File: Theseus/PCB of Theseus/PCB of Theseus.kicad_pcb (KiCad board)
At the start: 2 copper layers, 135 x 80 mm, 127 parts, among them J1 TB001-500-04BE, J11 TB002-500-02BE, J12 TB002-500-02BE, J2 TB001-500-04BE, J3 TB002-500-02BE, J4 TB003-500-P06BE, J5 CN4 STDC14 (Programmer), J6 Micro SD Holder 0472192001, J7 TB002-500-02BE, J8 TB003-500-P06BE, Q1 DMG1012UW-7, Q2 DMG1012UW-7, U1 TPS565201DDC, U11 INA326, U12 INA326, U13 MAX6675, U2 MCP2562, U3 INA326, U4 INA326, U5 MX25L25645G, U6 STM32H750VBTx, Y1 ASE-4.000MHz-L-C-T

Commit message: Flight design, first pass
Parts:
- removed C20, C21: 0.5n, Capacitor_SMD:C_0805_2012Metric_Pad1.18x1.45mm_HandSolder
- removed C23, C28, C29, C34: 0.47u, Capacitor_SMD:C_0805_2012Metric_Pad1.18x1.45mm_HandSolder
- removed C27, C33: 0.047u, Capacitor_SMD:C_0805_2012Metric_Pad1.18x1.45mm_HandSolder
- removed C30, C31: 2n, Capacitor_SMD:C_0805_2012Metric_Pad1.18x1.45mm_HandSolder
- removed C36, C37, C38, C39: 0.1u, Capacitor_SMD:C_0805_2012Metric_Pad1.18x1.45mm_HandSolder
- removed J11, J12: TB002-500-02BE, TerminalBlock_CUI:TerminalBlock_CUI_TB007-508-02_1x02_P5.08mm_Horizontal
- removed J8: TB003-500-P06BE, TerminalBlock_CUI:TerminalBlock_CUI_TB007-508-06_1x06_P5.08mm_Horizontal
- removed R18, R19: 32.4k ±0.1%, Resistor_SMD:R_0805_2012Metric_Pad1.20x1.40mm_HandSolder
- removed R20: 100R ±0.1%, Resistor_SMD:R_0805_2012Metric_Pad1.20x1.40mm_HandSolder
- removed R21, R38: 8.06k, Resistor_SMD:R_0805_2012Metric_Pad1.20x1.40mm_HandSolder
- removed R22, R23: 200k, Resistor_SMD:R_0805_2012Metric_Pad1.20x1.40mm_HandSolder
- removed R24, R25, R30: 1M ±0.1%, Resistor_SMD:R_0805_2012Metric_Pad1.20x1.40mm_HandSolder
- removed R26, R31, R32, R37: 806R, Resistor_SMD:R_0805_2012Metric_Pad1.20x1.40mm_HandSolder
- removed R29: 10M ±1%, Resistor_SMD:R_0805_2012Metric_Pad1.20x1.40mm_HandSolder
- removed R33, R35: 20k, Resistor_SMD:R_0805_2012Metric_Pad1.20x1.40mm_HandSolder
- removed R34, R36: 80.6k, Resistor_SMD:R_0805_2012Metric_Pad1.20x1.40mm_HandSolder
- removed TH1: PTS060301B100RP100, Resistor_SMD:R_0603_1608Metric_Pad0.98x0.95mm_HandSolder
- removed TP2: TC2+, TestPoint:TestPoint_Pad_D2.0mm
- removed TP3: TC2-, TestPoint:TestPoint_Pad_D2.0mm
- removed TP6: TC3+, TestPoint:TestPoint_Pad_D2.0mm
- removed TP7: TC3-, TestPoint:TestPoint_Pad_D2.0mm
- removed TP8: RTD1, TestPoint:TestPoint_Pad_D2.0mm
- removed TP9: RTD2, TestPoint:TestPoint_Pad_D2.0mm
- removed U11, U12, U3, U4: INA326, Package_SO:MSOP-8_3x3mm_P0.65mm
- C1, C2, C22, C25, C3, C32, C6, C7, C8, D1, D5, L1, Q1, Q2, R1, R11, R12, R2, R27, R28, R3, R46, R47, R5, R6, U1, U2: moved to B.Cu
- C26: moved to F.Cu
- J1, J2: value TB001-500-04BE -> Conn_01x06_Socket; footprint TerminalBlock_CUI:TerminalBlock_CUI_TB007-508-04_1x04_P5.08mm_Horizontal -> canhw_footprints:connector_Harwin_G125–MG10605M4P
- J3: value TB002-500-02BE -> G125-MH104M4-04AD000P; footprint TerminalBlock_CUI:TerminalBlock_CUI_TB007-508-02_1x02_P5.08mm_Horizontal -> canhw_footprints:connector_Harwin_G125-MH104M4-04AD000P
- J4: value TB003-500-P06BE -> Conn_01x06_Socket; footprint TerminalBlock_CUI:TerminalBlock_CUI_TB007-508-06_1x06_P5.08mm_Horizontal -> canhw_footprints:connector_Harwin_G125–MG10605M4P
- R13, R14, R15, R16, R17: value 50k -> 51k
- moved H6 101.0 mm to (184.3, 49.8)
- moved J7 86.1 mm to (182.0, 64.0), turned to 90 degrees
- moved TP10 85.8 mm to (175.8, 74.5), turned to 0 degrees
- moved H8 85.2 mm to (123.2, 89.1)
- moved TP1 84.6 mm to (175.6, 69.8), turned to 0 degrees
- moved L1 84.5 mm to (169.9, 82.7), turned to 180 degrees
- moved R11 79.5 mm to (169.9, 78.8), turned to 0 degrees
- moved C3 76.9 mm to (170.0, 75.5), turned to 0 degrees
- moved D5 75.7 mm to (141.3, 90.8)
- moved G*** 75.1 mm to (182.4, 72.8), turned to 90 degrees
- moved J1 71.5 mm to (138.2, 87.3)
- moved R12 71.4 mm to (170.9, 67.1), turned to 0 degrees
- moved D1 71.2 mm to (136.1, 90.8)
- moved U1 71.1 mm to (169.9, 71.1), turned to 0 degrees
- moved C24 70.8 mm to (166.6, 50.1)
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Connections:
- J2 pad 1: +5V -> +3.3V
- J2 pad 2: GND -> /MCU/HALL_1
- J2 pad 3: /CANH -> GND
- J2 pad 4: /CANL -> +3.3V
- J3 pad 1: Net-(J3-Pin_1) -> /CANH
- J3 pad 2: Net-(J3-Pin_2) -> /CANL
- TP4 pad 1: Net-(J12-Pin_2) -> /Valves and Sensors/TC1+
- TP5 pad 1: Net-(J12-Pin_1) -> /Valves and Sensors/TC1-
- U13 pad 2: Net-(J12-Pin_2) -> /Valves and Sensors/TC1+
- U13 pad 3: Net-(J12-Pin_1) -> /Valves and Sensors/TC1-
- U6 pad 1: /MCU/TC2+ -> unconnected-(U6-PE2-Pad1)
- U6 pad 2: /MCU/TC2- -> unconnected-(U6-PE3-Pad2)
- U6 pad 3: /MCU/TC3 -> unconnected-(U6-PE4-Pad3)
- U6 pad 35: /MCU/PT_2 -> /MCU/PT_1
- U6 pad 36: /MCU/PT_1 -> /MCU/PT_2
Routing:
- net +BATT: track 180.9 -> 76.7 mm, vias 0 -> 2
- net /MCU/VALVE_2: track 61.2 -> 5.38 mm, vias 0 -> 1
- net /MCU/TC3: track 43.4 -> 0.00 mm
- net /MCU/VALVE_1: track 43.7 -> 5.40 mm, vias 0 -> 1
- net /Valves and Sensors/TC1+: track 0.00 -> 31.3 mm
- net Net-(C21-Pad2): track 25.1 -> 0.00 mm
- net /MCU/TCK: track 13.4 -> 37.4 mm
- net +3.3V: track 152.3 -> 128.5 mm, vias 29 -> 14
- net /MCU/TC2+: track 23.0 -> 0.00 mm
- net /MCU/V_BATT: track 60.7 -> 37.8 mm, vias 0 -> 1
- net /CAN_Rx: track 27.1 -> 4.45 mm, vias 0 -> 1
- net GND: track 128.5 -> 148.5 mm, vias 11 -> 19
- net /CAN_Tx: track 22.6 -> 3.60 mm, vias 0 -> 1
- net /MCU/OSC_IN: track 22.7 -> 4.25 mm
- net /Valves and Sensors/TC1-: track 0.00 -> 18.2 mm
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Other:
- board size 135 x 80 mm -> 72.5 x 50 mm
- board text added: "PCB OF THESEUS FLIGHT EDITION REV 3"
- board text removed: "+3.3V"
- board text removed: "3.3V"
- board text removed: "5V"
- board text removed: "BATT+"
- board text removed: "CANH"
- board text removed: "CANL"
- board text removed: "CLK"
- board text removed: "DI"
- board text removed: "DO"
- board text removed: "GND"
- board text removed: "HALL"
- board text removed: "HALL 1"
- board text removed: "HALL 2"
- board text removed: "IF YOU'RE READING THIS THE PCB IS UPSIDE-DOWN (OR YOU'RE IN THE SHADOW REALM)"
- board text removed: "PCB OF THESEUS DEV EDITION, REV 2"
- board text removed: "PT1+"
- board text removed: "PT1-"
- board text removed: "PT2+"
- board text removed: "PT2-"
- board text removed: "PT3+"
- board text removed: "PT3-"
- board text removed: "RST"
- board text removed: "RTD+"
- board text removed: "RTD-"
- board text removed: "TC1+"
- board text removed: "TC1-"
- board text removed: "TC2+"
- board text removed: "TC2-"
- board text removed: "TC3+"
- board text removed: "TC3-"
- board text removed: "TMS"
- board text removed: "V1+"
- board text removed: "V1-"
- board text removed: "V2+"
- board text removed: "V2-"
- board text removed: "VCP_RX"
- board text removed: "VCP_TX"

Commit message: Flight design v1
First pass at flight design
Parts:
- removed the G*** at (182.4, 72.8)
- removed the G*** at (152.1, 50.5)
- removed J4: Conn_01x06_Socket, canhw_footprints:connector_Harwin_G125–MG10605M4P
- added G***: LOGO, Team_Logo:Logo_SilkScreen_5mm, F.Cu at (152.9, 111.5)
- added J8: Conn_01x12_Socket, canhw_footprints:connector_Harwin_G125-MV11205M1P, F.Cu at (139.5, 117.5)
- added R10: 82K, Resistor_SMD:R_0603_1608Metric_Pad0.98x0.95mm_HandSolder, F.Cu at (145.1, 112.8)
- added R18: 130K, Resistor_SMD:R_0603_1608Metric_Pad0.98x0.95mm_HandSolder, B.Cu at (146.7, 112.8)
- added R19: 82K, Resistor_SMD:R_0603_1608Metric_Pad0.98x0.95mm_HandSolder, F.Cu at (142.3, 112.4)
- added R20: 130K, Resistor_SMD:R_0603_1608Metric_Pad0.98x0.95mm_HandSolder, B.Cu at (144.2, 112.9)
- added R8: 82K, Resistor_SMD:R_0603_1608Metric_Pad0.98x0.95mm_HandSolder, F.Cu at (147.2, 112.9)
- added R9: 130K, Resistor_SMD:R_0603_1608Metric_Pad0.98x0.95mm_HandSolder, B.Cu at (149.4, 112.9)
- C1, C11, C12, C16, C18, C19, C2, C24, C25, C3, C32, C35, C4, C5, C6: footprint Capacitor_SMD:C_0805_2012Metric_Pad1.18x1.45mm_HandSolder -> Capacitor_SMD:C_0603_1608Metric_Pad1.08x0.95mm_HandSolder
- C10, C13, C14, C15, C17, C26, C40, C9: footprint Capacitor_SMD:C_0805_2012Metric_Pad1.18x1.45mm_HandSolder -> Capacitor_SMD:C_0603_1608Metric_Pad1.08x0.95mm_HandSolder; moved to B.Cu
- C22, C7, C8: footprint Capacitor_SMD:C_0805_2012Metric_Pad1.18x1.45mm_HandSolder -> Capacitor_SMD:C_0603_1608Metric_Pad1.08x0.95mm_HandSolder; moved to F.Cu
- D2, D6: footprint Diode_SMD:D_1206_3216Metric_Pad1.42x1.75mm_HandSolder -> Diode_SMD:D_0603_1608Metric_Pad1.05x0.95mm_HandSolder
- F1, FB1, U13, U5, Y1: moved to B.Cu
- J5: footprint Connector_PinHeader_1.27mm:PinHeader_2x07_P1.27mm_Vertical_SMD -> Connector_PinSocket_1.27mm:PinSocket_2x07_P1.27mm_Vertical_SMD
- J7: value TB002-500-02BE -> 4DB-P108-02; footprint TerminalBlock_CUI:TerminalBlock_CUI_TB007-508-02_1x02_P5.08mm_Horizontal -> canhw_footprints:4DB-P108-02
- Q1, Q2: moved to F.Cu
- R1, R11, R12, R13, R14, R15, R16, R17, R2, R3, R4, R7: footprint Resistor_SMD:R_0805_2012Metric_Pad1.20x1.40mm_HandSolder -> Resistor_SMD:R_0603_1608Metric_Pad0.98x0.95mm_HandSolder
- R27, R28, R5, R6: footprint Resistor_SMD:R_0805_2012Metric_Pad1.20x1.40mm_HandSolder -> Resistor_SMD:R_0603_1608Metric_Pad0.98x0.95mm_HandSolder; moved to F.Cu
- R44, R45: footprint Resistor_SMD:R_0805_2012Metric_Pad1.20x1.40mm_HandSolder -> Resistor_SMD:R_0603_1608Metric_Pad0.98x0.95mm_HandSolder; moved to B.Cu
- R46: value 3M ±1% -> 300K; footprint Resistor_SMD:R_0805_2012Metric_Pad1.20x1.40mm_HandSolder -> Resistor_SMD:R_0603_1608Metric_Pad0.98x0.95mm_HandSolder
- R47: value 1M ±0.1% -> 100K; footprint Resistor_SMD:R_0805_2012Metric_Pad1.20x1.40mm_HandSolder -> Resistor_SMD:R_0603_1608Metric_Pad0.98x0.95mm_HandSolder
- moved H6 90.1 mm to (121.0, 114.0)
- moved H5 85.1 mm to (179.0, 114.0)
- moved C16 68.2 mm to (161.6, 118.0), turned to 0 degrees
- moved C24 65.2 mm to (165.2, 115.3), turned to 0 degrees
- moved C4 63.8 mm to (165.2, 118.0), turned to 0 degrees
- moved C17 61.8 mm to (130.6, 105.1), turned to 0 degrees
- moved C5 61.0 mm to (161.6, 115.3), turned to 180 degrees
- moved C11 60.2 mm to (137.6, 110.5), turned to 0 degrees
- moved C35 58.1 mm to (124.7, 92.4)
- moved C12 57.9 mm to (151.1, 107.2), turned to 0 degrees
- moved R46 57.3 mm to (152.4, 117.0), turned to 90 degrees
- moved C26 57.3 mm to (162.1, 106.8), turned to 180 degrees
- moved R47 56.3 mm to (152.4, 112.6), turned to 90 degrees
- moved C40 53.4 mm to (141.5, 99.1), turned to 0 degrees
- moved TP1 48.1 mm to (168.6, 117.4)
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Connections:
- net /MCU/PT_3 renamed /Valves and Sensors/PT3_OUT
- R1 pad 1: /MCU/PT_1 -> /Valves and Sensors/PT1_OUT
- R2 pad 1: /MCU/PT_2 -> /Valves and Sensors/PT2_OUT
- U6 pad 35: /MCU/PT_1 -> /Valves and Sensors/PT2_OUT
- U6 pad 36: /MCU/PT_2 -> /Valves and Sensors/PT1_OUT
- U6 pad 40: unconnected-(U6-PE10-Pad40) -> /MCU/PT6
- U6 pad 41: unconnected-(U6-PE11-Pad41) -> /MCU/PT5
- U6 pad 42: unconnected-(U6-PE12-Pad42) -> /MCU/PT4
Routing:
- net GND: track 148.5 -> 34.1 mm, vias 19 -> 9
- net +BATT: track 76.7 -> 130.2 mm, vias 2 -> 0
- net /MCU/VCP_RX: track 5.05 -> 36.8 mm, vias 0 -> 2
- net +3.3V: track 128.5 -> 100.5 mm, vias 14 -> 24
- net /MCU/TCK: track 37.4 -> 12.3 mm, vias 2 -> 0
- net +5V: track 42.8 -> 17.7 mm
- net /CANL: track 26.6 -> 2.66 mm
- net /MCU/PT_1: track 23.9 -> 0.00 mm, vias 1 -> 0
- net /MCU/VCP_TX: track 7.69 -> 30.9 mm, vias 0 -> 2
- net /MCU/TMS: track 32.4 -> 9.97 mm, vias 0 -> 2
- net /CANH: track 25.1 -> 2.67 mm
- net /MCU/SD_CMD: track 22.4 -> 44.6 mm
- net /MCU/PT_2: track 21.8 -> 0.00 mm, vias 1 -> 0
- net /MCU/SD_D3: track 19.0 -> 40.2 mm
- net /MCU/V_BATT: track 37.8 -> 17.6 mm
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- added copper zone on In2.Cu, net +3.3V
- added copper zone on B.Cu, net GND
- added copper zone on In1.Cu, net GND
- removed copper zone on B.Cu, net +3.3V
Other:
- board size 72.5 x 50 mm -> 70 x 40 mm
- copper layers 2 -> 4
- board text added: "PCB OF THESEUS REV 3 MATTHEW GORDON"
- board text added: "TCK"
- board text added: "TDI"
- board text added: "TDO"
- board text added: "TMS"
- board text added: "TRST"
- board text added: "VALVE 1"
- board text added: "VALVE 2"
- board text added: "VCPRX"
- board text added: "VCPTX"
- board text removed: "MATTHEW GORDON"
- board text removed: "PCB OF THESEUS FLIGHT EDITION REV 3"

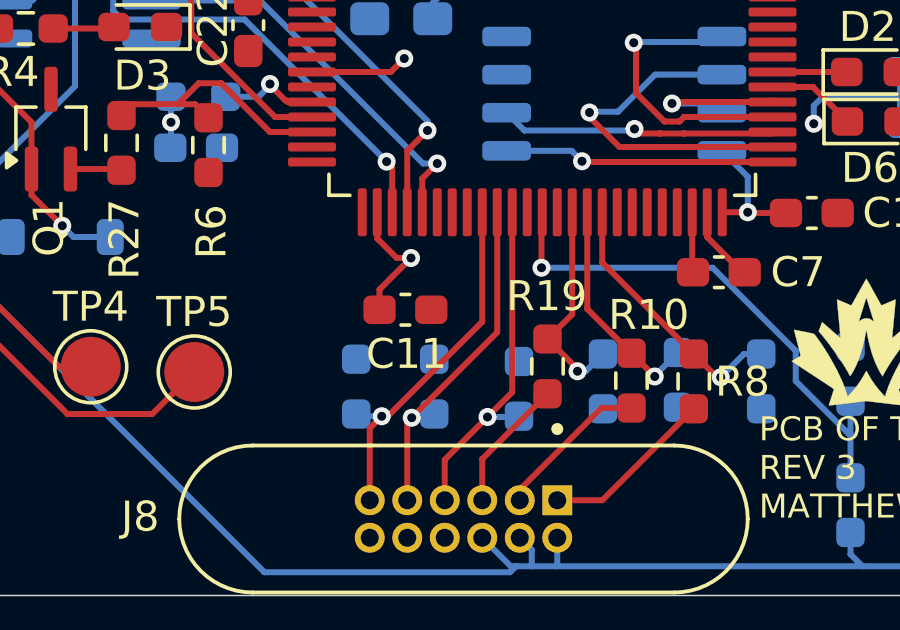
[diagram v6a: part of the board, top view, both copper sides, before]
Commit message: Fix PT3 ADC
Updated PT3 to use valid ADC pin
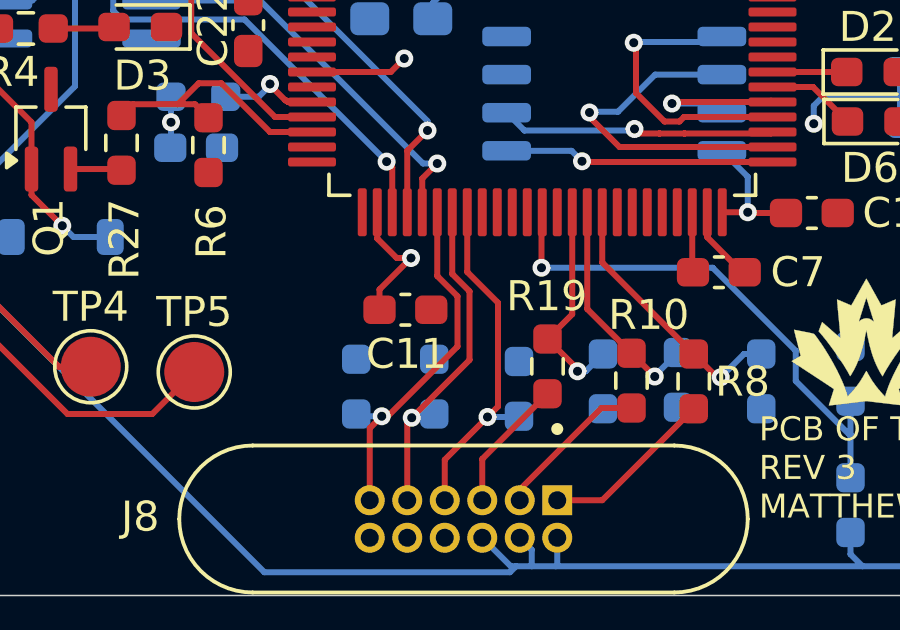
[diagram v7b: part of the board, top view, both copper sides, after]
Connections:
- U6 pad 31: unconnected-(U6-PA7-Pad31) -> /Valves and Sensors/PT3_OUT
- U6 pad 32: unconnected-(U6-PC4-Pad32) -> /Valves and Sensors/PT2_OUT
- U6 pad 33: unconnected-(U6-PC5-Pad33) -> /Valves and Sensors/PT1_OUT
- U6 pad 34: /Valves and Sensors/PT3_OUT -> unconnected-(U6-PB0-Pad34)
- U6 pad 35: /Valves and Sensors/PT2_OUT -> unconnected-(U6-PB1-Pad35)
- U6 pad 36: /Valves and Sensors/PT1_OUT -> unconnected-(U6-PB2-Pad36)
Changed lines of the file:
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@@
 	(net 42 "Net-(U1-VBST)")
 	(net 43 "unconnected-(U6-PC3_C-Pad18)")
-	(net 44 "unconnected-(U6-PC5-Pad33)")
+	(net 44 "unconnected-(U6-PB0-Pad34)")
 	(net 45 "unconnected-(U6-PB7-Pad93)")
 	(net 46 "unconnected-(U6-PC0-Pad15)")
-	(net 47 "unconnected-(U6-PC4-Pad32)")
+	(net 47 "unconnected-(U6-PB2-Pad36)")
 	(net 48 "unconnected-(U6-PE0-Pad97)")
 	(net 49 "unconnected-(U6-PA11-Pad70)")
@@
 	(net 90 "unconnected-(U6-PE7-Pad37)")
 	(net 91 "unconnected-(U6-PE4-Pad3)")
-	(net 92 "unconnected-(U6-PA7-Pad31)")
+	(net 92 "unconnected-(U6-PB1-Pad35)")
 	(net 93 "unconnected-(U6-PA2-Pad24)")
 	(net 94 "unconnected-(J3-NC-Pad4)")
@@
 			(layers "F.Cu" "F.Mask" "F.Paste")
 			(roundrect_rratio 0.25)
-			(net 92 "unconnected-(U6-PA7-Pad31)")
+			(net 114 "/Valves and Sensors/PT3_OUT")
 			(pinfunction "PA7")
-			(pintype "bidirectional+no_connect")
+			(pintype "bidirectional")
 		)
 		(pad "32" smd roundrect
@@
 			(layers "F.Cu" "F.Mask" "F.Paste")
 			(roundrect_rratio 0.25)
-			(net 47 "unconnected-(U6-PC4-Pad32)")
+			(net 113 "/Valves and Sensors/PT2_OUT")
 			(pinfunction "PC4")
-			(pintype "bidirectional+no_connect")
+			(pintype "bidirectional")
 		)
 		(pad "33" smd roundrect
@@
 			(layers "F.Cu" "F.Mask" "F.Paste")
 			(roundrect_rratio 0.25)
-			(net 44 "unconnected-(U6-PC5-Pad33)")
+			(net 112 "/Valves and Sensors/PT1_OUT")
 			(pinfunction "PC5")
-			(pintype "bidirectional+no_connect")
+			(pintype "bidirectional")
 		)
 		(pad "34" smd roundrect
@@
 			(layers "F.Cu" "F.Mask" "F.Paste")
 			(roundrect_rratio 0.25)
-			(net 114 "/Valves and Sensors/PT3_OUT")
+			(net 44 "unconnected-(U6-PB0-Pad34)")
 			(pinfunction "PB0")
-			(pintype "bidirectional")
+			(pintype "bidirectional+no_connect")
 		)
 		(pad "35" smd roundrect
@@
 			(layers "F.Cu" "F.Mask" "F.Paste")
 			(roundrect_rratio 0.25)
-			(net 113 "/Valves and Sensors/PT2_OUT")
+			(net 92 "unconnected-(U6-PB1-Pad35)")
 			(pinfunction "PB1")
-			(pintype "bidirectional")
+			(pintype "bidirectional+no_connect")
 		)
 		(pad "36" smd roundrect
@@
 			(layers "F.Cu" "F.Mask" "F.Paste")
 			(roundrect_rratio 0.25)
-			(net 112 "/Valves and Sensors/PT1_OUT")
+			(net 47 "unconnected-(U6-PB2-Pad36)")
 			(pinfunction "PB2")
-			(pintype "bidirectional")
+			(pintype "bidirectional+no_connect")
 		)
 		(pad "37" smd roundrect
@@
 	)
 	(segment
-		(start 141.15 113.225)
-		(end 141.15 107.225)
+		(start 140.325 114.05)
+		(end 138.9 115.475)
+		(width 0.2)
+		(layer "F.Cu")
+		(net 112)
+	)
+	(segment
+		(start 138.9 115.475)
+		(end 138.9 116.825)
 		(width 0.2)
 		(layer "F.Cu")
@@
 	(segment
 		(start 140.325 114.05)
-		(end 138.9 115.475)
+		(end 140.675 113.7)
 		(width 0.2)
 		(layer "F.Cu")
@@
 	)
 	(segment
-		(start 138.9 115.475)
-		(end 138.9 116.825)
+		(start 140.675 110.2408)
+		(end 140.675 113.7)
 		(width 0.2)
 		(layer "F.Cu")
@@
 	)
 	(segment
-		(start 140.325 114.05)
-		(end 141.15 113.225)
+		(start 139.65 107.225)
+		(end 139.65 109.2158)
+		(width 0.2)
+		(layer "F.Cu")
+		(net 112)
+	)
+	(segment
+		(start 139.65 109.2158)
+		(end 140.675 110.2408)
 		(width 0.2)
 		(layer "F.Cu")
@@
 	)
 	(segment
-		(start 140.65 111.225)
-		(end 140.65 107.225)
+		(start 139.15 107.225)
+		(end 139.15 109.2829)
+		(width 0.2)
+		(layer "F.Cu")
+		(net 113)
+	)
+	(segment
+		(start 139.726 109.8589)
+		(end 139.726 112.149)
 		(width 0.2)
 		(layer "F.Cu")
@@
 	(segment
 		(start 137.8 114.075)
-		(end 140.65 111.225)
+		(end 139.726 112.149)
 		(width 0.2)
 		(layer "F.Cu")
@@
 	)
 	(segment
+		(start 139.15 109.2829)
+		(end 139.726 109.8589)
+		(width 0.2)
+		(layer "F.Cu")
+		(net 113)
+	)
+	(segment
 		(start 137.8 114.075)
 		(end 137.65 114.225)
@@
 	)
 	(segment
+		(start 139.325 111.7)
+		(end 137 114.025)
+		(width 0.2)
+		(layer "F.Cu")
+		(net 114)
+	)
+	(segment
+		(start 139.325 110.025)
+		(end 139.325 111.7)
+		(width 0.2)
+		(layer "F.Cu")
+		(net 114)
+	)
+	(segment
 		(start 137 114.025)
 		(end 136.8 114.025)
@@
 	)
 	(segment
-		(start 140.15 110.875)
-		(end 137 114.025)
+		(start 138.65 109.35)
+		(end 139.325 110.025)
 		(width 0.2)
 		(layer "F.Cu")
@@
 	)
 	(segment
-		(start 140.15 107.225)
-		(end 140.15 110.875)
+		(start 138.65 107.225)
+		(end 138.65 109.35)
 		(width 0.2)
 		(layer "F.Cu")

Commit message: 10-MAR-2026 Revisions
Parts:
- C25, C6: value 10u -> 0.1u
- R12: value 10.2k -> 10k
- moved C3 17.1 mm to (163.2, 97.1), turned to -90 degrees
- moved R11 16.7 mm to (170.7, 95.9), turned to 180 degrees
- moved U1 16.0 mm to (166.0, 98.0), turned to -90 degrees
- moved L1 15.7 mm to (168.7, 92.9), turned to 180 degrees
- moved R12 13.4 mm to (170.7, 97.7), turned to 0 degrees
- moved C2 12.3 mm to (168.6, 100.5), turned to 90 degrees
- moved C1 9.76 mm to (170.1, 100.5), turned to 90 degrees
- moved F1 8.29 mm to (170.6, 105.0), turned to -90 degrees
- moved C32 7.78 mm to (171.6, 100.5), turned to 90 degrees
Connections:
- J1 pad 6: /Valves and Sensors/TC1- -> GND
- TP5 pad 1: /Valves and Sensors/TC1- -> GND
- U13 pad 2: /Valves and Sensors/TC1+ -> GND
- U13 pad 3: /Valves and Sensors/TC1- -> /Valves and Sensors/TC1+
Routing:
- net GND: track 34.1 -> 85.9 mm, vias 9 -> 12
- net /Valves and Sensors/TC1-: track 31.6 -> 0.00 mm, vias 1 -> 0
- net +BATT: track 130.2 -> 125.2 mm
- net Net-(U1-SW): track 11.3 -> 6.99 mm
- net +3.3V: track 100.5 -> 102.5 mm, vias 24 -> 23
- net Net-(U1-VBST): track 5.45 -> 3.46 mm
- net Net-(J7-Pin_1): track 3.04 -> 4.92 mm
- net Net-(U1-VFB): track 4.49 -> 5.92 mm
- net Net-(D1-A): track 13.1 -> 14.5 mm
- net /Valves and Sensors/TC1+: track 33.7 -> 32.4 mm
